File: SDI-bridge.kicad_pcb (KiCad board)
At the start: 6 copper layers, 68 x 33 mm, 195 parts, among them J1 031-70526-21, J2 031-70526-21, J3 WE_68715014522_ONE-SIDE, J4 MC-HVT1-S04-G, J5 MC-HVT1-S04-G, U1 MAX8902B, U2 GS2971A, U3 GS2988, U4 CrossLink_LIF-MD6000-6JMG80I, U5 SC18IS602BIPW, Y1 ABM7_27.000MH_D2Y_T

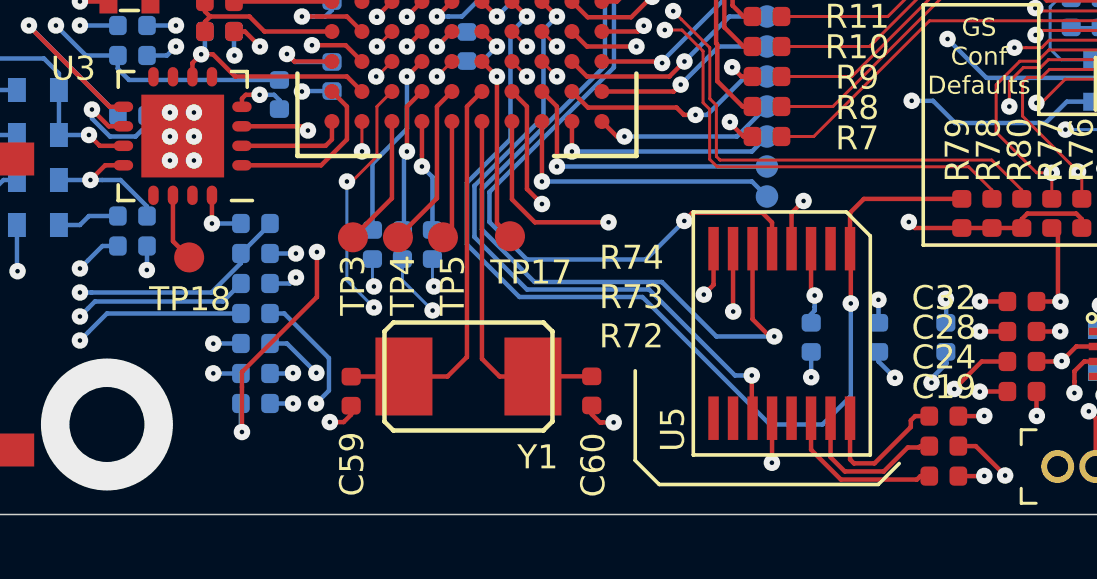
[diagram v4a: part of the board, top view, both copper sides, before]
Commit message: Add I2S connector and GND planes
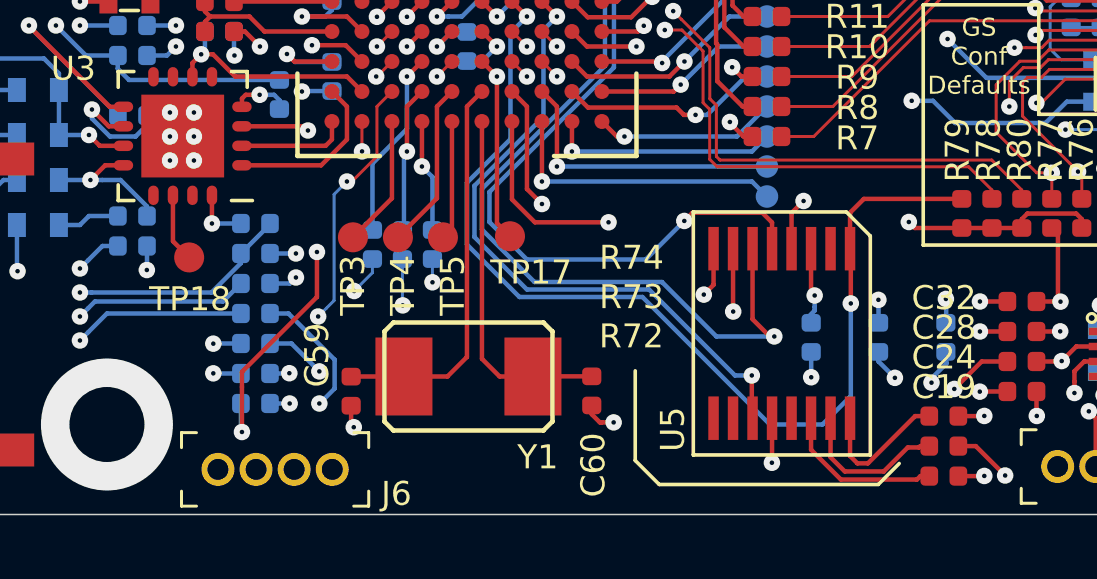
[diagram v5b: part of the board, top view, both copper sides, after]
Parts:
- added J6: MC-HVT1-S04-G, antmicro-footprints:PinHeader_1x4_P1.27mm_Drill.7mm, F.Cu at (112.7, 131.5)
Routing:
- net /AUDIO_OUTPUT_CH1_2: track 37.3 -> 46.6 mm
- net /AUDIO_WORD_CLK: track 29.9 -> 38.9 mm
- net /AUDIO_MASTER_CLK: track 28.1 -> 37.0 mm
- net /AUDIO_SERIAL_BIT_CLK: track 30.1 -> 37.2 mm
- added copper zone on In2.Cu, net (none)
- added copper zone on In3.Cu, net GNDREF
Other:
- net class Default: trace_width 0.125 -> 0.1
